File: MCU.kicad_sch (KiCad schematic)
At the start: 0 parts

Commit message: Schematic progress.
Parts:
- added C16, C17, C18, C19, C32, C33: 100n, Capacitor_SMD:C_0603_1608Metric_Pad1.08x0.95mm_HandSolder, symbol Device:C
- added C21, C23, C25, C27: 10n, Capacitor_SMD:C_0603_1608Metric_Pad1.08x0.95mm_HandSolder, symbol Device:C
- added C22, C24, C26, C28: 100p, Capacitor_SMD:C_0603_1608Metric_Pad1.08x0.95mm_HandSolder, symbol Device:C
- added C30, C31, C34: 10u, Capacitor_SMD:C_0603_1608Metric_Pad1.08x0.95mm_HandSolder, symbol Device:C
- added D1, D2: 1N4148W, Diode_SMD:D_SOD-123, symbol Diode:1N4148W
- added J1: Conn_Coaxial, Connector_Coaxial:BNC_Amphenol_B6252HB-NPP3G-50_Horizontal, symbol Connector:Conn_Coaxial
- added J6: USB_B, Connector_USB:USB_B_OST_USB-B1HSxx_Horizontal, symbol Connector:USB_B
- added R20, R22, R23, R25, R27, R34: 100, Resistor_SMD:R_0603_1608Metric_Pad0.98x0.95mm_HandSolder, symbol Device:R
- added R21, R24, R26, R28: 10k, Resistor_SMD:R_0603_1608Metric_Pad0.98x0.95mm_HandSolder, symbol Device:R
- added SW1, SW2: RotaryEncoder_Switch, DC_load:rotary_encoder_bottom_solder, symbol Device:RotaryEncoder_Switch
- added U1, U10, U11, U12: FSA3157P6X, Package_TO_SOT_SMD:SOT-363_SC-70-6_Handsoldering, symbol Analog_Switch:FSA3157P6X
- added U14: AMS1117-3.3, Package_TO_SOT_SMD:SOT-223-3_TabPin2, symbol Regulator_Linear:AMS1117-3.3
- added U15: 74HC14D653, Package_SO:SOIC-14_3.9x8.7mm_P1.27mm, symbol 74xx:74HC14
- added U16: LM4040DBZ-3, Package_TO_SOT_SMD:SOT-23, symbol Reference_Voltage:LM4040DBZ-3
- added U2: Screen, PID_lib:WC1602A - below, symbol DC_load:2x16_screen
- added U8: STM32F103C8Tx, Package_QFP:LQFP-48_7x7mm_P0.5mm, symbol MCU_ST_STM32F1:STM32F103C8Tx
- added U9: CH340C, Package_SO:SOIC-16_3.9x9.9mm_P1.27mm, symbol Interface_USB:CH340C
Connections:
- new net: C21.2, R21.2, R22.1
- new net: C27.2, R27.1, R28.2
- new net: R27.2, U15.2
- new net: C25.2, R25.1, R26.2
- new net: R25.2, U15.12
- new net: C23.2, R23.1, R24.2
- new net: J1.1 (In), R20.1
- new net: J6.3 (D+), U9.5 (UD+)
- new net: J6.2 (D-), U9.6 (UD-)
- new net: R22.2, U15.8
- new net: R23.2, U15.10
- new net: U8.23 (VSS), U8.35 (VSS), U8.47 (VSS)
- new net +5V: C31.1, J6.1 (VBUS), R34.2, U14.3 (VI), U9.16 (VCC)
- new net 3V3: C30.1, D2.1 (K), U14.2 (VO), U8.24 (VDD), U8.36 (VDD), U8.48 (VDD)
- new net 5V: C16.2, C17.2, C18.2, C19.2, U1.5 (V+), U10.5 (V+), U11.5 (V+), U12.5 (V+)
- new net BNC_CONTROL: D1.1 (K), D2.2 (A), R20.2, U1.1, U10.1, U11.1, U12.1
- new net CH1_CONTROL: U1.4
- new net CH1_MCU_CONTROL: C22.2, R21.1, U1.3
- new net CH1_PWM: U15.9
- new net CH1_SEL: U1.6
- new net CH2_CONTROL: U10.4
- new net CH2_MCU_CONTROL: C24.2, R24.1, U10.3
- new net CH2_PWM: U15.11
- new net CH2_SEL: U10.6
- new net CH3_CONTROL: U11.4
- new net CH3_MCU_CONTROL: C26.2, R26.1, U11.3
- new net CH3_PWM: U15.13
- new net CH3_SEL: U11.6
- new net CH4_CONTROL: U12.4
- new net CH4_MCU_CONTROL: C28.2, R28.1, U12.3
- new net CH4_PWM: U15.1
- new net CH4_SEL: U12.6
- new net GND: C16.1, C17.1, C18.1, C19.1, C21.1, C22.1, C23.1, C24.1, C25.1, C26.1, C27.1, C28.1, C30.2, C31.2, C32.1, C33.1, C34.2, D1.2 (A), J1.2 (Ext), J6.4 (GND), J6.5 (Shield), U1.2 (GND), U10.2 (GND), U11.2 (GND), U12.2 (GND), U14.1 (GND), U15.3, U15.5, U15.7 (GND), U16.2 (A), U9.1 (GND)
- new net VREF: C32.2, C33.2, C34.1, R34.1, U15.14 (VCC), U16.1 (K), U8.9 (VDDA)

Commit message: aesthetics.
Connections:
- net BNC_CONTROL: now also R20.1; no longer R20.2
- net at J1.1 (In): now also R20.2; no longer R20.1
- net CH1_MCU_CONTROL: no longer names the net of C22.2, R21.1, U1.3
- net CH2_MCU_CONTROL: no longer names the net of C24.2, R24.1, U10.3
- net CH3_MCU_CONTROL: no longer names the net of C26.2, R26.1, U11.3
- net CH4_MCU_CONTROL: no longer names the net of C28.2, R28.1, U12.3
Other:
- moved on the sheet: C16, C17, C18, C19, C21, C22, C23, C24, C25, C26, C27, C28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

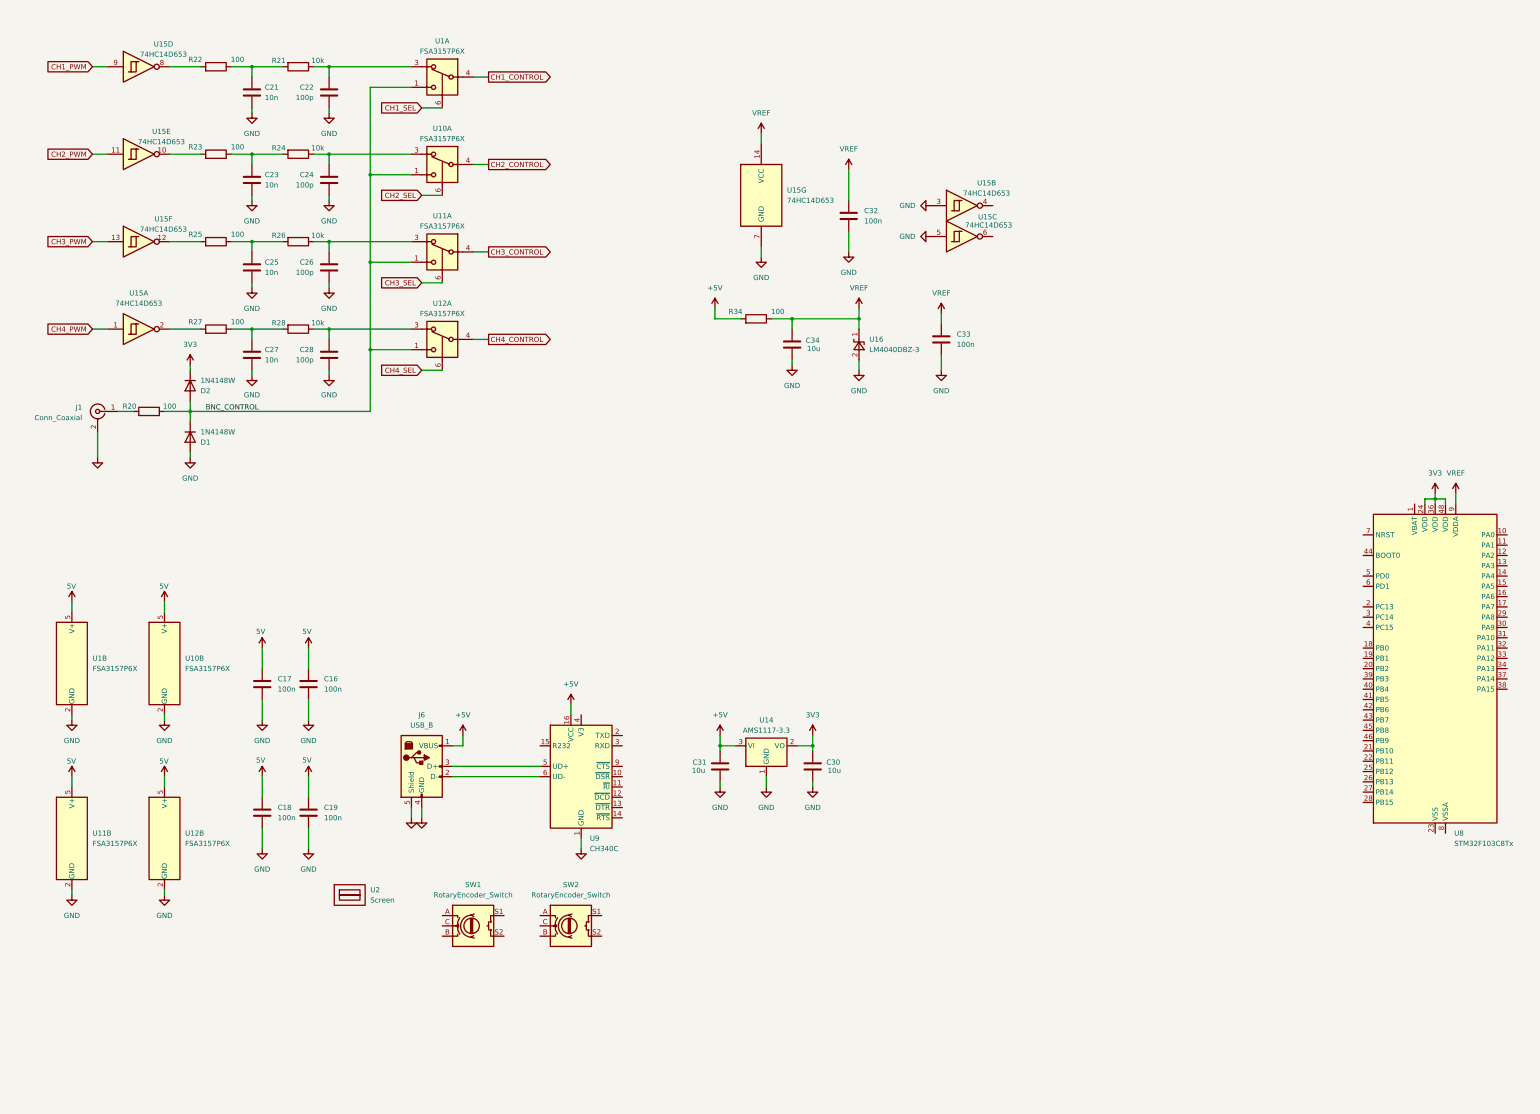
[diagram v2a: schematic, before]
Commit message: Schematic and placement update.
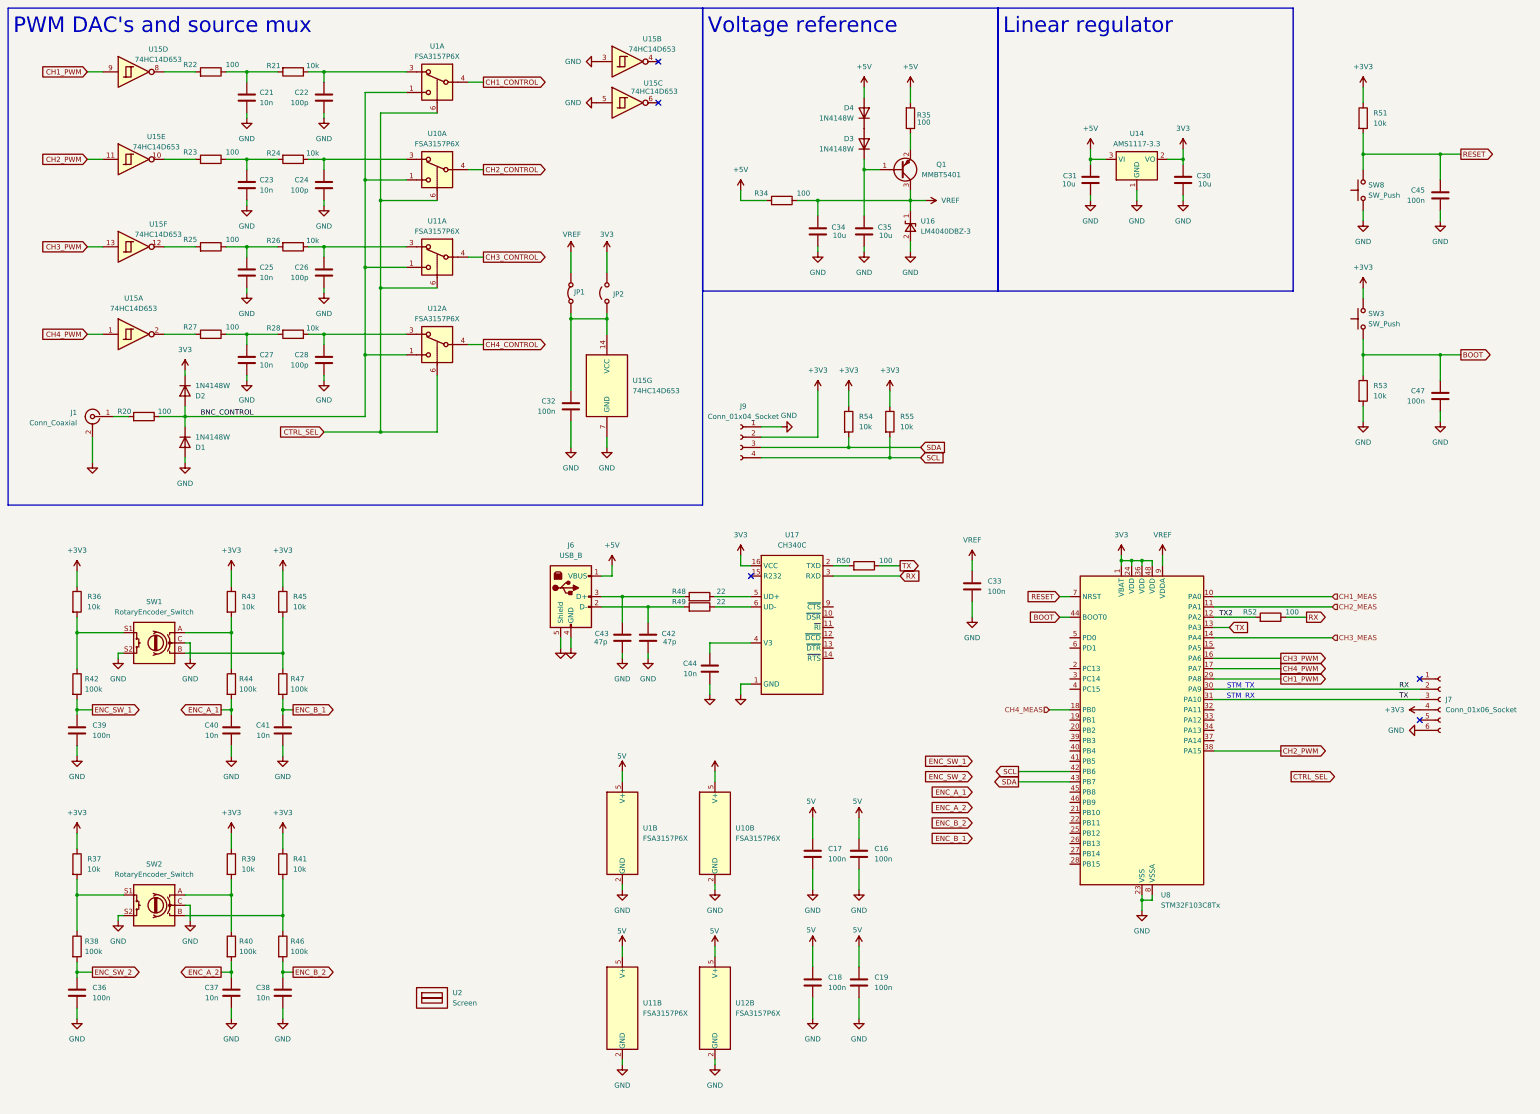
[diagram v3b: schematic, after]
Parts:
- removed U9: CH340C, Package_SO:SOIC-16_3.9x9.9mm_P1.27mm, symbol Interface_USB:CH340C
- added C35: 10u, Capacitor_SMD:C_0603_1608Metric_Pad1.08x0.95mm_HandSolder, symbol Device:C
- added C36, C39, C45, C47: 100n, Capacitor_SMD:C_0603_1608Metric_Pad1.08x0.95mm_HandSolder, symbol Device:C
- added C37, C38, C40, C41, C44: 10n, Capacitor_SMD:C_0603_1608Metric_Pad1.08x0.95mm_HandSolder, symbol Device:C
- added C42, C43: 47p, Capacitor_SMD:C_0603_1608Metric_Pad1.08x0.95mm_HandSolder, symbol Device:C
- added D3, D4: 1N4148W, Diode_SMD:D_SOD-123, symbol Diode:1N4148W
- added J7: Conn_01x06_Socket, Connector_PinSocket_2.54mm:PinSocket_1x06_P2.54mm_Vertical, symbol Connector:Conn_01x06_Socket
- added J9: Conn_01x04_Socket, Connector_PinSocket_2.54mm:PinSocket_1x04_P2.54mm_Vertical, symbol Connector:Conn_01x04_Socket
- added JP1: Jumper_2_Bridged, Jumper:SolderJumper-2_P1.3mm_Bridged_RoundedPad1.0x1.5mm, symbol Jumper:Jumper_2_Bridged
- added JP2: Jumper_2_Open, Jumper:SolderJumper-2_P1.3mm_Open_RoundedPad1.0x1.5mm, symbol Jumper:Jumper_2_Open
- added Q1: MMBT5401, Package_TO_SOT_SMD:SOT-23, symbol Transistor_BJT:MMBT3906
- added R35, R50, R52: 100, Resistor_SMD:R_0603_1608Metric_Pad0.98x0.95mm_HandSolder, symbol Device:R
- added R36, R37, R39, R41, R43, R45, R51, R53, R54, R55: 10k, Resistor_SMD:R_0603_1608Metric_Pad0.98x0.95mm_HandSolder, symbol Device:R
- added R38, R40, R42, R44, R46, R47: 100k, Resistor_SMD:R_0603_1608Metric_Pad0.98x0.95mm_HandSolder, symbol Device:R
- added R48, R49: 22, Resistor_SMD:R_0603_1608Metric_Pad0.98x0.95mm_HandSolder, symbol Device:R
- added SW3, SW8: SW_Push, Button_Switch_THT:SW_TH_Tactile_Omron_B3F-10xx, symbol Switch:SW_Push
- added U17: CH340C, Package_SO:SOIC-16_3.9x9.9mm_P1.27mm, symbol DC_load:CH340C
- U14: LCSC (none) -> C6186
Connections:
- net CH2_SEL is gone; now on net CTRL_SEL: U10.6
- net CH3_SEL is gone; now on net CTRL_SEL: U11.6
- net CH4_SEL is gone; now on net CTRL_SEL: U12.6
- net +5V: now also D4.2 (A), R35.2
- net 3V3: now also U8.1 (VBAT), JP2.2 (B), U17.16 (VCC)
- net CH1_PWM: now also U8.29 (PA8)
- net CH2_PWM: now also U8.38 (PA15)
- net CH3_PWM: now also U8.16 (PA6)
- net CH4_PWM: now also U8.17 (PA7)
- net GND: now also SW1.C, SW1.S2, SW2.C, SW2.S2, U8.23 (VSS), U8.35 (VSS), U8.47 (VSS), U8.8 (VSSA), C35.2, C36.1, C37.1, C38.1, C39.1, C40.1, C41.1, C42.2, C43.2, C44.1, C45.1, C47.1, J7.6 (Pin_6), J9.1 (Pin_1), R53.2, SW8.1, U17.1 (GND)
- net VREF: now also JP1.2 (B), Q1.3 (C); no longer C32.2, U15.14 (VCC)
- net at J6.3 (D+): now also C43.1, R48.2
- net at J6.2 (D-): now also C42.1, R49.2
- net at SW1.A: now also R43.2, R44.1
- net at SW1.B: now also R45.2, R47.1
- net at SW1.S1: now also R36.2, R42.1
- net CH1_MEAS: now reaches U8.10 (PA0)
- net CH2_MEAS: now reaches U8.11 (PA1)
- net TX2: now reaches U8.12 (PA2)
- net TX2: now also R52.2
- net TX: now reaches U8.13 (PA3)
- net TX: now also U8.31 (PA10), J7.3 (Pin_3), R50.1
- net CH3_MEAS: now reaches U8.14 (PA4)
- net CH4_MEAS: now reaches U8.18 (PB0)
- net RX: now reaches U8.30 (PA9)
- net RX: now also J7.2 (Pin_2), R52.1, U17.3 (RXD)
- net SCL: now reaches U8.42 (PB6)
- net SCL: now also J9.4 (Pin_4), R55.2
- net SDA: now reaches U8.43 (PB7)
- net SDA: now also J9.3 (Pin_3), R54.2
- net BOOT: now reaches U8.44 (BOOT0)
- net BOOT: now also C47.2, R53.1, SW3.1
- net RESET: now reaches U8.7 (NRST)
- net RESET: now also C45.2, R51.2, SW8.2
- net at SW2.A: now also R39.2, R40.1
- net at SW2.B: now also R41.2, R46.1
- net at SW2.S1: now also R37.2, R38.1
- net CH1_SEL renamed CTRL_SEL
- new net: C32.2, JP1.1 (A), JP2.1 (A), U15.14 (VCC)
- new net: C35.1, D3.1 (K), Q1.1 (B)
- new net: D3.2 (A), D4.1 (K)
- new net: C44.2, U17.4 (V3)
- new net: R49.1, U17.6 (UD-)
- new net: Q1.2 (E), R35.1
- new net: R48.1, U17.5 (UD+)
- new net: R50.2, U17.2 (TXD)
- new net +3V3: J7.4 (Pin_4), J9.2 (Pin_2), R36.1, R37.1, R39.1, R41.1, R43.1, R45.1, R51.1, R54.1, R55.1, SW3.2
- new net ENC_A_1: C40.2, R44.2
- new net ENC_A_2: C37.2, R40.2
- new net ENC_B_1: C41.2, R47.2
- new net ENC_B_2: C38.2, R46.2
- new net ENC_SW_1: C39.2, R42.2
- new net ENC_SW_2: C36.2, R38.2
- no-connect marks 0 -> 5
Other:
- note added: "Linear regulator"
- note added: "PWM DAC's and source mux"
- note added: "STM_RX"
- note added: "STM_TX"
- note added: "Voltage reference"
- moved on the sheet: C16, C17, C18, C19, C21, C22, C23, C24, C25, C26, C27, C28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
